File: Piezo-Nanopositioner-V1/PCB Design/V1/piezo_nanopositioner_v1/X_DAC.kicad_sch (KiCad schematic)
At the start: 29 parts, among them J4 Conn_01x10_Pin, J5 RF2-04A-T-00-50-G, U3 TL431AIDBZR, U5 DAC0800LCM, U6 TDA2050

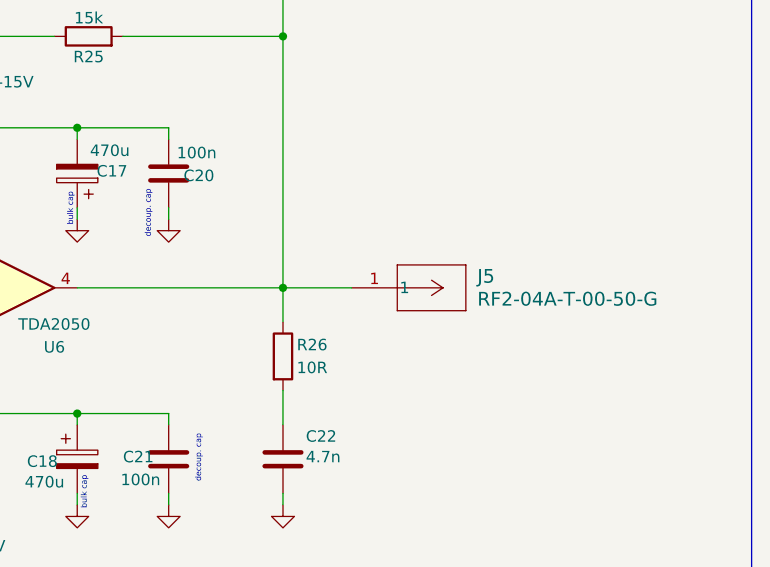
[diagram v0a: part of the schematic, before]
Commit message: started PCB design, almost finished first DAC.
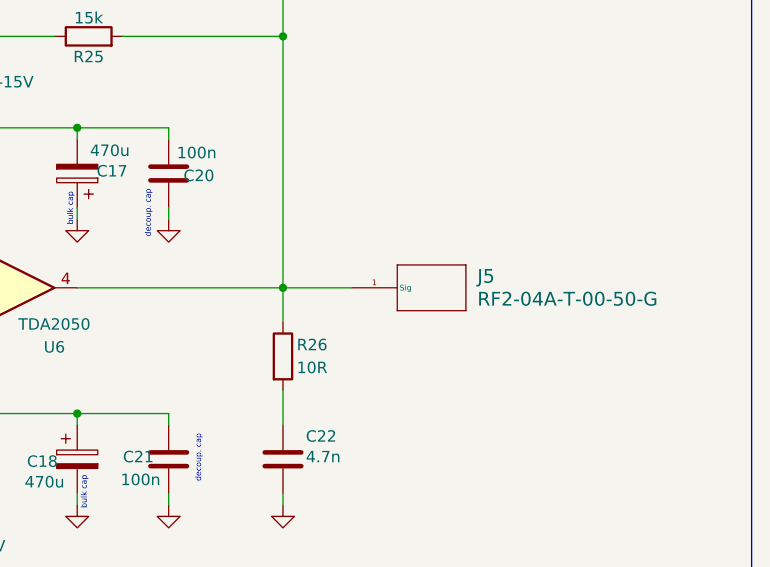
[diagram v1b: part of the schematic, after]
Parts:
- J5: footprint RF:CONN_RF2-04A-T-00-50-G_ADM -> CONN_RF2-04A-T-00-50-G_ADM
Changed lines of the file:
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@@
-	)
-	(symbol
-		(lib_id "SMA_Connector:RF2-04A-T-00-50-G")
-		(at 220.98 102.87 0)
-		(unit 1)
-		(exclude_from_sim no)
-		(in_bom yes)
-		(on_board yes)
-		(dnp no)
-		(fields_autoplaced yes)
-		(property "Reference" "J5"
-			(at 234.95 101.5999 0)
-			(effects
-				(font
-					(size 1.524 1.524)
-				)
-				(justify left)
-			)
-		)
-		(property "Value" "RF2-04A-T-00-50-G"
-			(at 234.95 104.1399 0)
-			(effects
-				(font
-					(size 1.524 1.524)
-				)
-				(justify left)
-			)
-		)
-		(property "Footprint" "RF:CONN_RF2-04A-T-00-50-G_ADM"
-			(at 220.98 102.87 0)
-			(effects
-				(font
-					(size 1.27 1.27)
-					(italic yes)
-				)
-				(hide yes)
-			)
-		)
-		(property "Datasheet" "RF2-04A-T-00-50-G"
-			(at 220.98 102.87 0)
-			(effects
-				(font
-					(size 1.27 1.27)
-					(italic yes)
-				)
-				(hide yes)
-			)
-		)
-		(property "Description" ""
-			(at 220.98 102.87 0)
-			(effects
-				(font
-					(size 1.27 1.27)
-				)
-				(hide yes)
-			)
-		)
-		(pin "1"
-		)
-		(instances
-			(project "piezo_nanopositioner_v1"
-				(path "/7b2a32d8-cc7d-471d-a8eb-eea62713ed45/d7b1beb2-d1b4-4fd6-841d-9655fbd1005d"
-					(reference "J5")
-					(unit 1)
-				)
-			)
-		)
 	)
 	(symbol
@@
 					(unit 1)
 				)
+			)
+		)
+	)
+	(symbol
+		(lib_id "SMA_Connector:RF2-04A-T-00-50-G")
+		(at 220.98 102.87 0)
+		(unit 1)
+		(exclude_from_sim no)
+		(in_bom yes)
+		(on_board yes)
+		(dnp no)
+		(fields_autoplaced yes)
+		(property "Reference" "J5"
+			(at 234.95 101.5999 0)
+			(effects
+				(font
+					(size 1.524 1.524)
+				)
+				(justify left)
+			)
+		)
+		(property "Value" "RF2-04A-T-00-50-G"
+			(at 234.95 104.1399 0)
+			(effects
+				(font
+					(size 1.524 1.524)
+				)
+				(justify left)
+			)
+		)
+		(property "Footprint" "CONN_RF2-04A-T-00-50-G_ADM"
+			(at 221.742 93.726 0)
+			(effects
+				(font
+					(size 1.27 1.27)
+					(italic yes)
+				)
+				(hide yes)
+			)
+		)
+		(property "Datasheet" "RF2-04A-T-00-50-G"
+			(at 213.36 105.664 0)
+			(effects
+				(font
+					(size 1.27 1.27)
+					(italic yes)
+				)
+				(hide yes)
+			)
+		)
+		(property "Description" ""
+			(at 220.98 102.87 0)
+			(effects
+				(font
+					(size 1.27 1.27)
+				)
+				(hide yes)
+			)
+		)
+		(pin "1"
+		)
+		(instances
+			(project "piezo_nanopositioner_v1"
+				(path "/7b2a32d8-cc7d-471d-a8eb-eea62713ed45/d7b1beb2-d1b4-4fd6-841d-9655fbd1005d"
+					(reference "J5")
+					(unit 1)
+				)

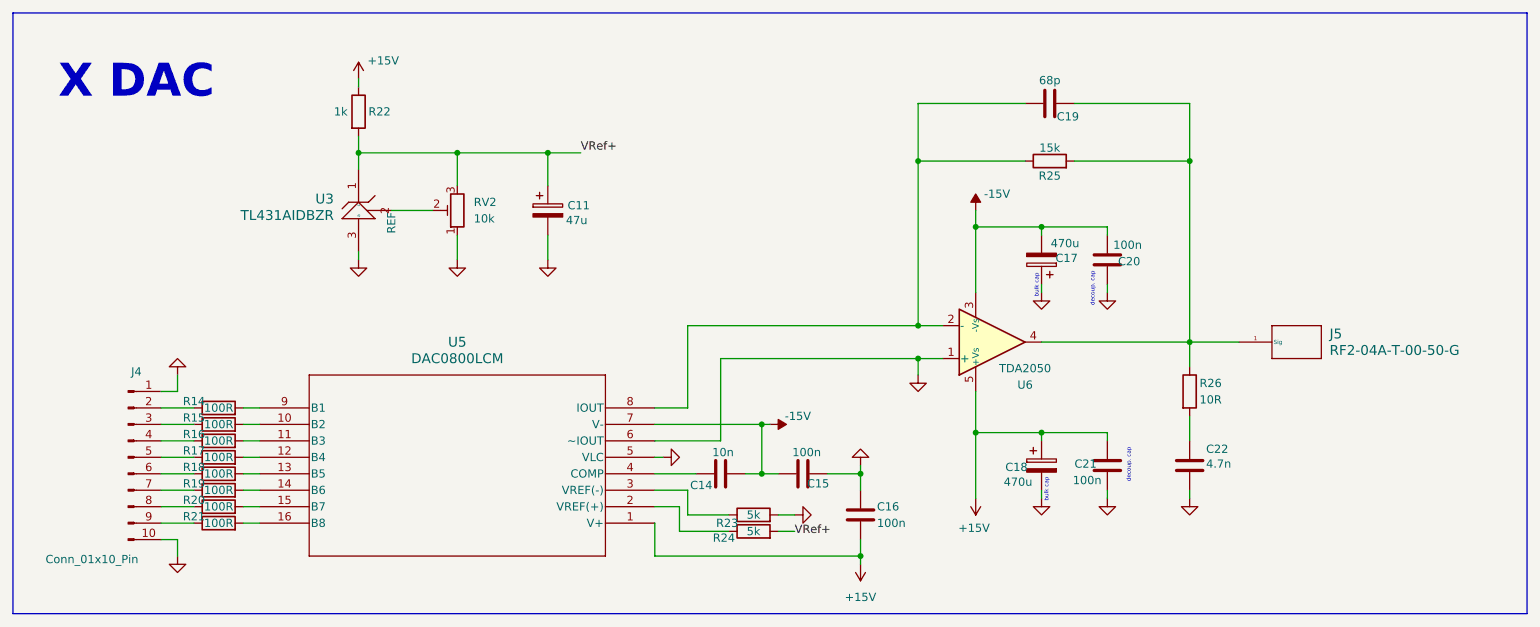
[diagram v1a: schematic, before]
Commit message: Created rough PCB component layout for Z actuator.
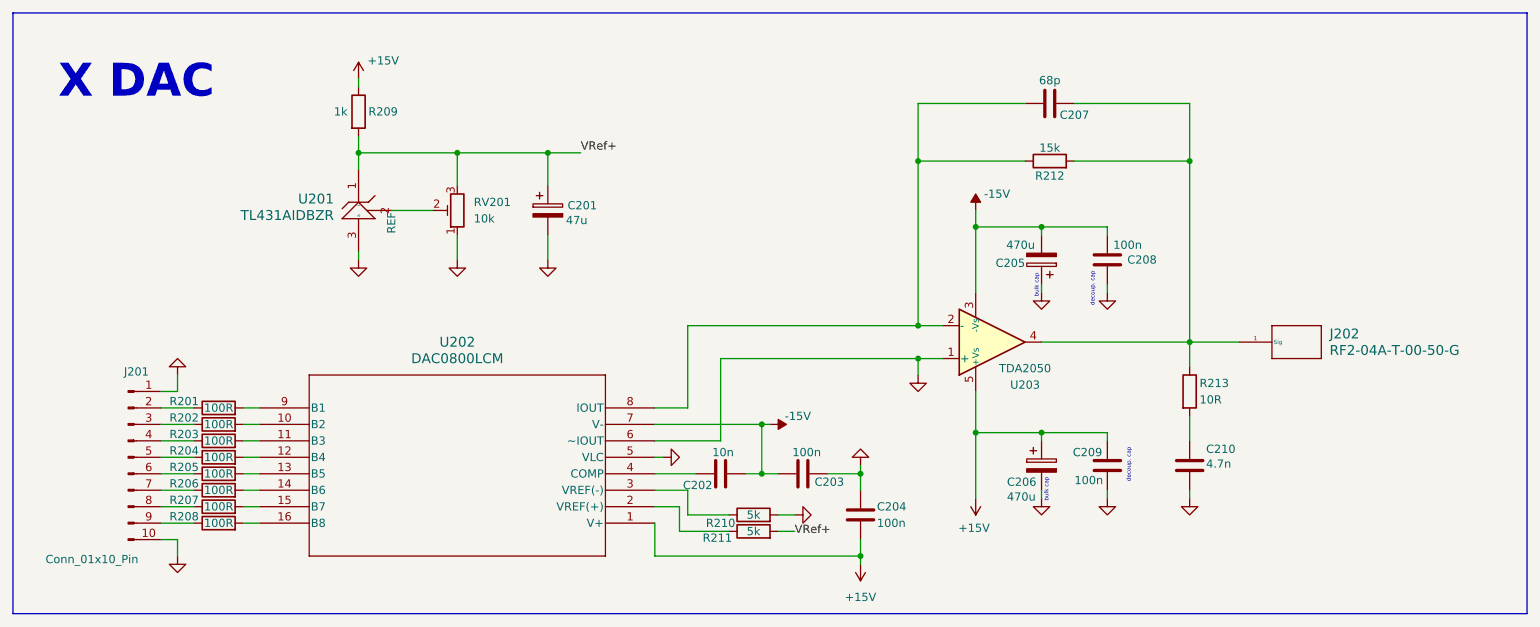
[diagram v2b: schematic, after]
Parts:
- renumbered C11 to C201, C14 to C202, C15 to C203, C16 to C204, C17 to C205, C18 to C206, C19 to C207, C20 to C208, C21 to C209, C22 to C210, J4 to J201, J5 to J202, R14 to R201, R15 to R202, R16 to R203, R17 to R204, R18 to R205, R19 to R206, R20 to R207, R21 to R208, R22 to R209, R23 to R210, R24 to R211, R25 to R212, R26 to R213, RV2 to RV201, U3 to U201, U5 to U202, U6 to U203

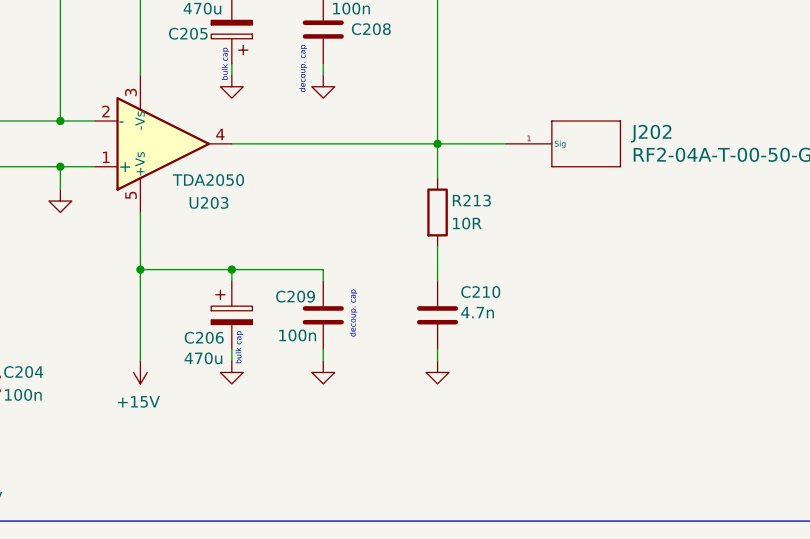
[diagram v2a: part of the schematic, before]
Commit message: added heatsink to XYZ schematics, finalized BOM, minimal PCB layout done.
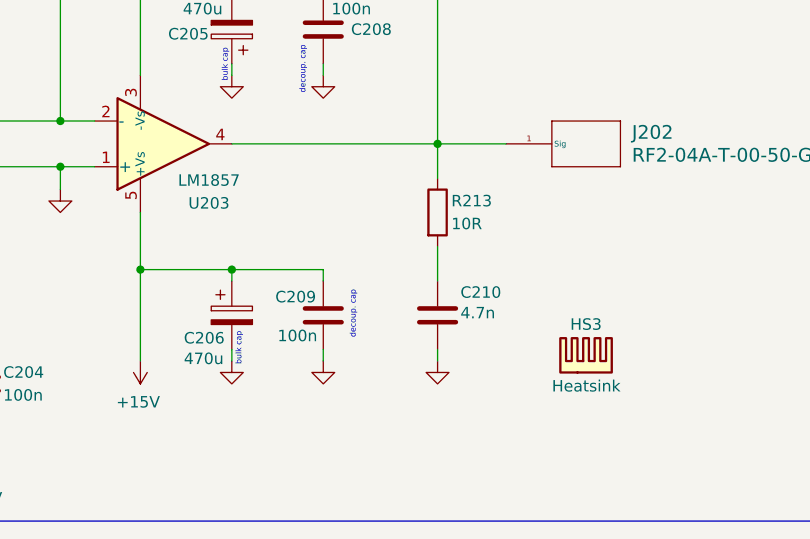
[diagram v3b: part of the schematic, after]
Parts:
- added HS3: Heatsink, V6560Y:V6560Y, symbol Mechanical:Heatsink
- C201: Distributor Link (none) -> https://www.digikey.ca/en/products/detail/panasonic-electro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; Manufacturer (none) -> Panasonic Electronic Components; Manufacturer Part (none) -> EEE-FC1E470P
- C202: Distributor Link (none) -> https://www.digikey.ca/en/products/detail/kemet/C0805C103F5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; Manufacturer (none) -> KEMET; Manufacturer Part (none) -> C0805C103F5GECAUTO
- C203, C204, C208, C209: Distributor Link (none) -> https://www.digikey.ca/en/products/detail/kemet/C0805C104K5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; Manufacturer (none) -> KEMET; Manufacturer Part (none) -> C0805C104K5RACTU
- C205, C206: Distributor Link (none) -> https://www.digikey.ca/en/products/detail/panasonic-electro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; Manufacturer (none) -> Panasonic Electronic Components; Manufacturer Part (none) -> EEH-ZS1E471P
- C207: Distributor Link (none) -> https://www.digikey.ca/en/products/detail/kemet/C0805C680K5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; Manufacturer (none) -> KEMET; Manufacturer Part (none) -> C0805C680K5GACTU
- C210: Distributor Link (none) -> https://www.digikey.ca/en/products/detail/kemet/C0805C472KD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; Manufacturer (none) -> KEMET; Manufacturer Part (none) -> C0805C472KDRACAUTO
- J201: Distributor Link (none) -> https://www.digikey.ca/en/products/detail/harwin-inc/M22-25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; Manufacturer (none) -> Harwin Inc.; Manufacturer Part (none) -> M22-2511005
- J202: Distributor Link (none) -> https://www.digikey.ca/en/products/detail/adam-tech/RF2-04A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; Manufacturer (none) -> Adam Tech; Manufacturer Part (none) -> RF2-04A-T-00-50-G
- R201, R202, R203, R204, R205, R206, R207, R208: Distributor Link (none) -> https://www.digikey.ca/en/products/detail/vishay-dale/CRCW0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; Manufacturer (none) -> Vishay Dale; Manufacturer Part (none) -> CRCW0805100RJNEC
- R209: Distributor Link (none) -> https://www.digikey.ca/en/products/detail/bourns-inc/CR0805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; Manufacturer (none) -> Bourns Inc.; Manufacturer Part (none) -> CR0805-JW-102ELF
- R210, R211: Distributor Link (none) -> https://www.digikey.ca/en/products/detail/te-connectivity-p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; Manufacturer (none) -> TE Connectivity Passive Product; Manufacturer Part (none) -> RLC73K2A1R0FTD
- R212: Distributor Link (none) -> https://www.digikey.ca/en/products/detail/rohm-semiconducto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; Manufacturer (none) -> Rohm Semiconductor; Manufacturer Part (none) -> ESR10EZPJ153
- R213: Distributor Link (none) -> https://www.digikey.ca/en/products/detail/bourns-inc/CR0805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; Manufacturer (none) -> Bourns Inc.; Manufacturer Part (none) -> CR0805AFX-10R0EAS
- RV201: Distributor Link (none) -> https://www.digikey.ca/en/products/detail/sparkfun-electron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; Manufacturer (none) -> SparkFun Electronics; Manufacturer Part (none) -> COM-09806
- U201: Distributor Link (none) -> https://www.digikey.ca/en/products/detail/texas-instruments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; Manufacturer (none) -> Texas Instruments; Manufacturer Part (none) -> TL431AIDBZR
- U202: Distributor Link (none) -> https://www.digikey.ca/en/products/detail/texas-instruments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; Manufacturer (none) -> Texas Instruments; Manufacturer Part (none) -> DAC0800LCM/NOPB
- U203: value TDA2050 -> LM1857; Distributor Link (none) -> https://www.digikey.com/en/products/detail/texas-instrument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; Manufacturer (none) -> Texas Instruments; Manufacturer Part (none) -> LM1875T/NOPB
